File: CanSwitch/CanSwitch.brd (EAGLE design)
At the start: 100 x 80 mm, 17 parts

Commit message: first attempt to do proper wiring on the board
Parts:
- XTAL: value (none) -> 16MHz; device led:LED5MM -> special:QS
- moved R2 7.18 mm to (34.3, 45.7), turned to 0 degrees
- moved R1 5.39 mm to (29.2, 55.9)
- moved STATUSLED 5.08 mm to (38.1, 6.35)
- moved DEBUGGING 3.81 mm to (55.9, 6.35)
- moved SWITCHINPUT 2.84 mm to (73.7, 16.5)
- moved CXT1 2.84 mm to (29.2, 31.8)
- moved C2 2.54 mm to (61.0, 29.2)
- moved CXT2 1.80 mm to (29.2, 24.1)
- moved MCP2561 1.27 mm to (73.7, 41.9)
- moved R3 1.27 mm to (31.8, 11.4)
- moved C1 1.27 mm to (22.9, 44.5)
- moved MCLR_J 1.27 mm to (22.9, 52.1)
- moved XTAL 1.27 mm to (38.1, 27.9), turned to 90 degrees
- moved C7 1.27 mm to (38.1, 39.4)
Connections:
- removed net N$5: CHIP.10, CXT2.2, XTAL.K
- new net N$3: CHIP.10, CXT2.2, XTAL.1
- net N$6: now also XTAL.2; no longer XTAL.A
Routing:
- net GND: track 0.00 -> 232.2 mm
- net PGC: track 0.00 -> 132.1 mm
- net +5V: track 0.00 -> 115.0 mm
- net PGD: track 0.00 -> 86.4 mm
- net MCLR: track 0.00 -> 65.0 mm
- net CANH: track 0.00 -> 64.9 mm
- net CANL: track 0.00 -> 58.7 mm
- net RXD: track 0.00 -> 30.7 mm
- net INPUT: track 0.00 -> 27.0 mm
- net TXD: track 0.00 -> 22.7 mm
- net N$7: track 0.00 -> 21.6 mm
- net N$3: track 0.00 -> 20.6 mm
- net N$6: track 0.00 -> 18.1 mm
- net N$4: track 0.00 -> 9.21 mm
- net N$2: track 0.00 -> 8.89 mm
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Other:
- board size 100 x 80 mm -> 64.8 x 78.7 mm

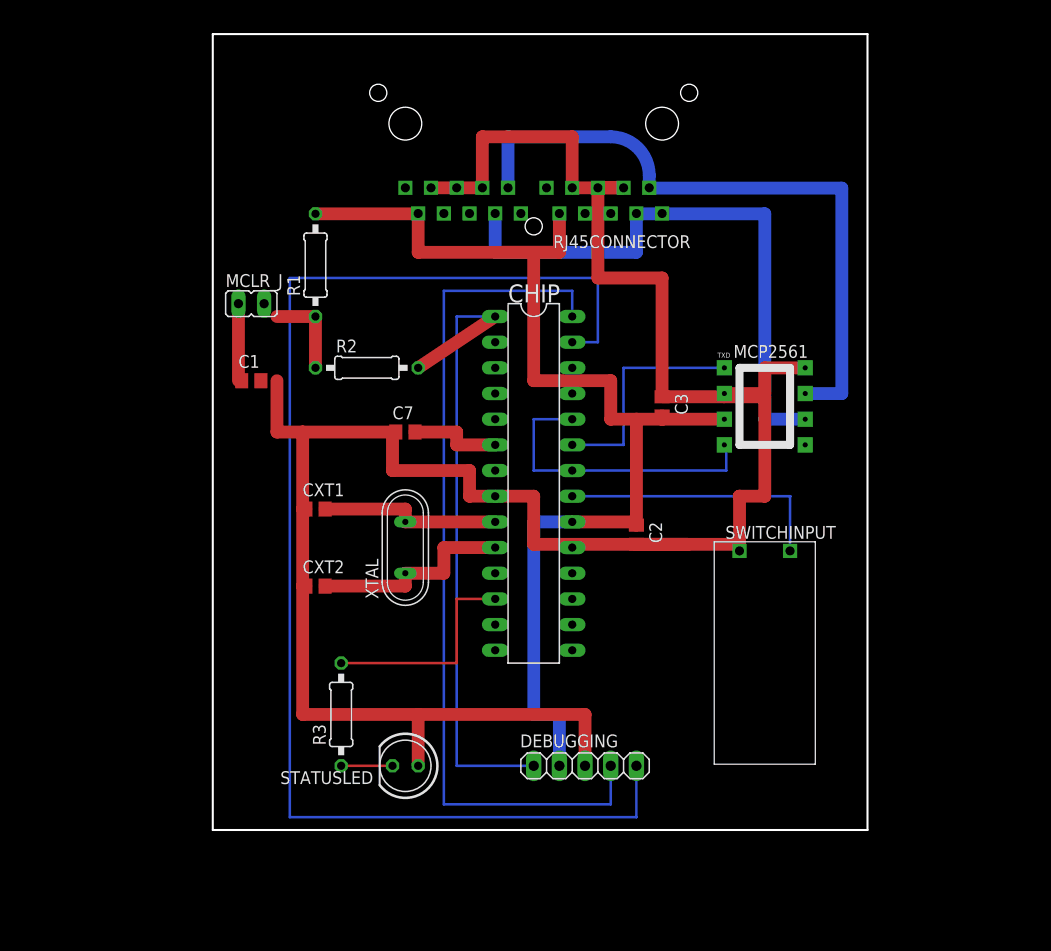
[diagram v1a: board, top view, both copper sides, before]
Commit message: cleanup after renaming libraries earlier this year and dropping auto routed nets in board to start from scratch again
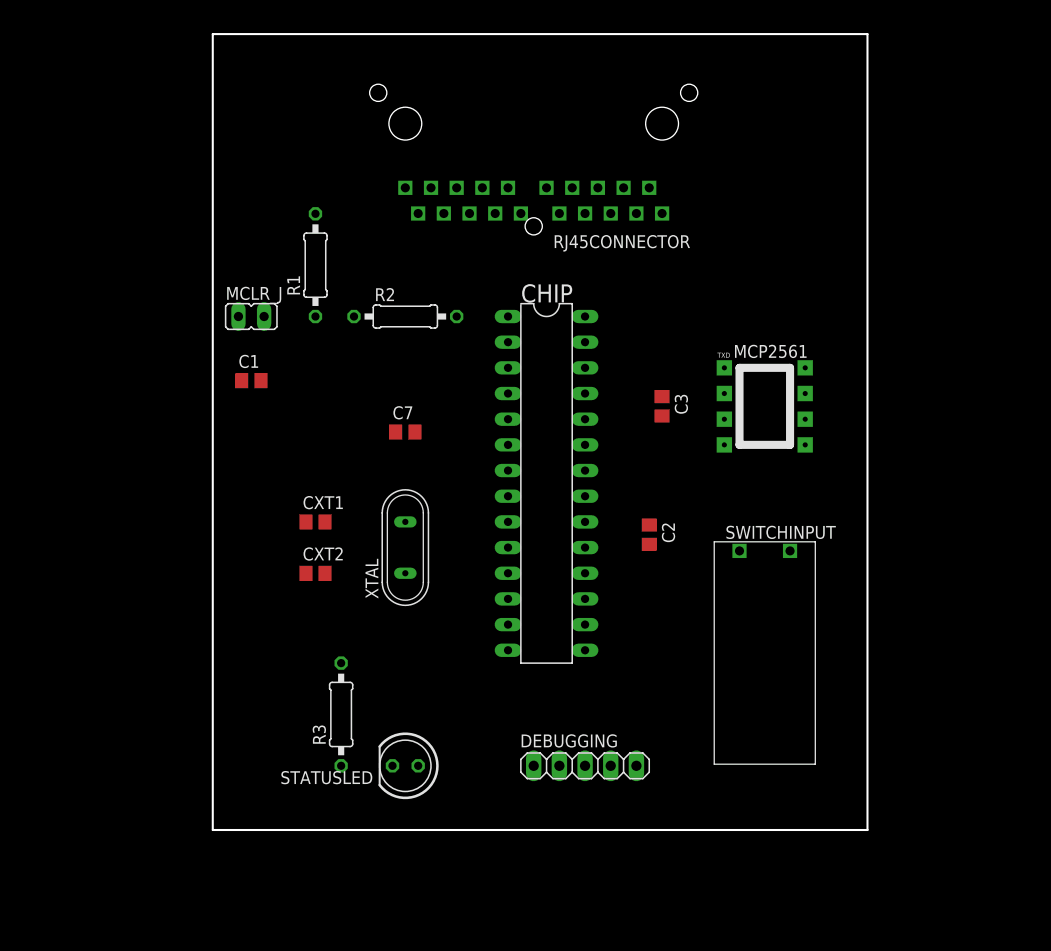
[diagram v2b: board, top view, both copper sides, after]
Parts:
- RJ45CONNECTOR: device GME:WEBP88_RJ45 -> PoJD:WEBP88_RJ45
- SWITCHINPUT: device GME:PTR_AK700_2_5.0 -> PoJD:PTR_AK700_2_5.0
- moved R2 6.35 mm to (38.1, 50.8)
- moved CHIP 1.27 mm to (52.1, 34.3)
- moved MCLR_J 1.27 mm to (22.9, 50.8)
- moved CXT1 1.27 mm to (29.2, 30.5)
- moved CXT2 1.27 mm to (29.2, 25.4)
- moved C2 1.27 mm to (62.2, 29.2)
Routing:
- net GND: track 232.2 -> 0.32 mm
- net PGC: track 132.1 -> 0.00 mm
- net +5V: track 115.0 -> 0.00 mm
- net PGD: track 86.4 -> 0.00 mm
- net CANH: track 64.9 -> 0.00 mm
- net MCLR: track 65.0 -> 0.90 mm
- net CANL: track 58.7 -> 0.00 mm
- net RXD: track 30.7 -> 0.00 mm
- net INPUT: track 27.0 -> 0.00 mm
- net TXD: track 22.7 -> 0.00 mm
- net N$7: track 21.6 -> 0.00 mm
- net N$3: track 20.6 -> 0.00 mm
- net N$6: track 18.1 -> 0.00 mm
- net N$4: track 9.21 -> 0.00 mm
- net N$2: track 8.89 -> 0.00 mm
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
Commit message: rerouting all, moving debugger up close to the chip, all check passed now
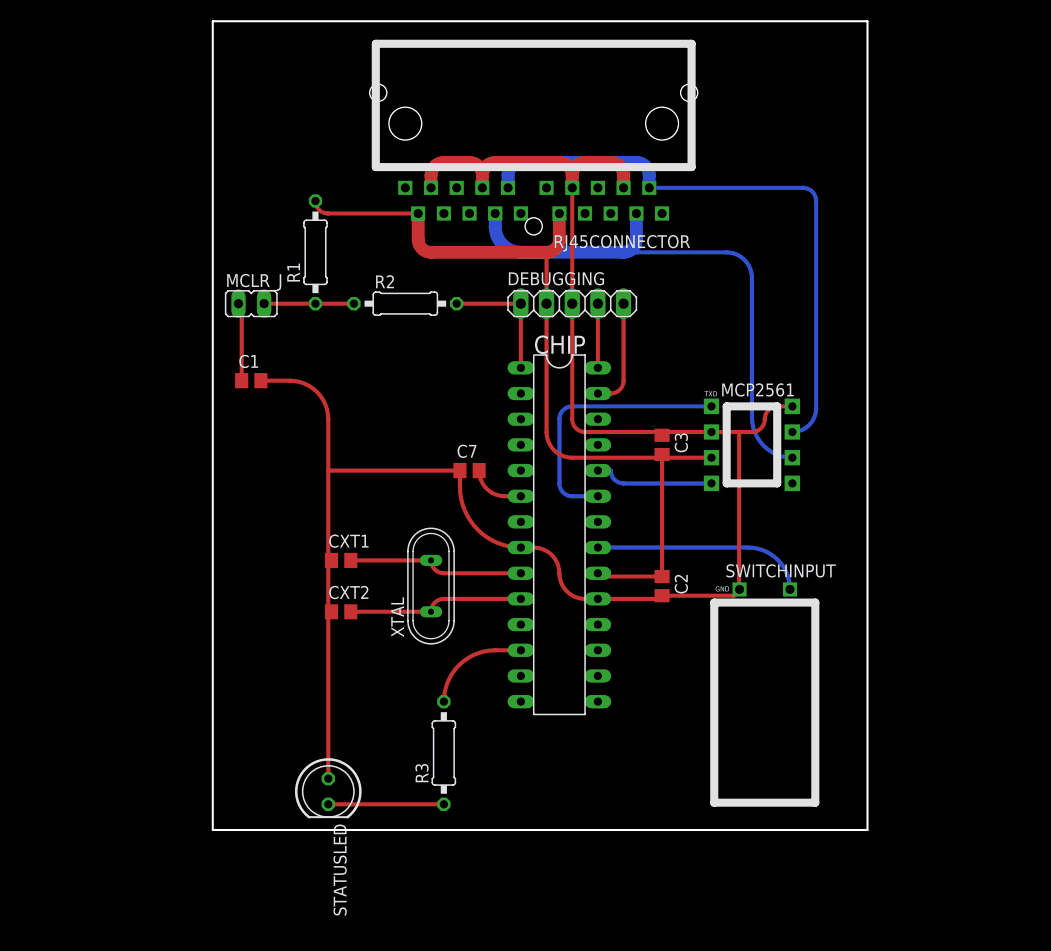
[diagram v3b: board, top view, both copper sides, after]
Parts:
- moved DEBUGGING 45.7 mm to (54.6, 52.1)
- moved R3 10.9 mm to (41.9, 7.62)
- moved STATUSLED 8.03 mm to (30.5, 3.81), turned to 270 degrees
- moved C7 7.41 mm to (44.5, 35.6)
- moved C2 5.24 mm to (63.5, 24.1)
- moved CHIP 5.24 mm to (53.3, 29.2)
- moved XTAL 4.58 mm to (40.6, 24.1)
- moved CXT1 4.58 mm to (31.8, 26.7)
- moved CXT2 4.58 mm to (31.8, 21.6)
- moved MCP2561 4.02 mm to (72.4, 38.1)
- moved SWITCHINPUT 3.81 mm to (73.7, 12.7)
- moved C3 3.81 mm to (63.5, 38.1)
- moved MCLR_J 1.27 mm to (22.9, 52.1)
- moved R2 1.27 mm to (38.1, 52.1)
- moved R1 1.27 mm to (29.2, 57.1)
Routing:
- net GND: track 0.32 -> 181.7 mm
- net +5V: track 0.00 -> 85.1 mm
- net CANH: track 0.00 -> 58.4 mm
- net CANL: track 0.00 -> 55.2 mm
- net TXD: track 0.00 -> 26.3 mm
- net INPUT: track 0.00 -> 20.7 mm
- net N$6: track 0.00 -> 17.4 mm
- net N$3: track 0.00 -> 17.4 mm
- net MCLR: track 0.90 -> 12.7 mm
- net RXD: track 0.00 -> 11.8 mm
- net N$8: track 0.00 -> 11.4 mm
- net PGC: track 0.00 -> 10.7 mm
- net N$7: track 0.00 -> 9.72 mm
- net N$2: track 0.00 -> 8.89 mm
- net N$1: track 0.32 -> 7.75 mm
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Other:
- board size 64.8 x 78.7 mm -> 64.8 x 80 mm
